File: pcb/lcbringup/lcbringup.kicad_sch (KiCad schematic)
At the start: 4 parts, among them M1 SCREWHOLE, M2 SCREWHOLE, M3 SCREWHOLE, M4 SCREWHOLE

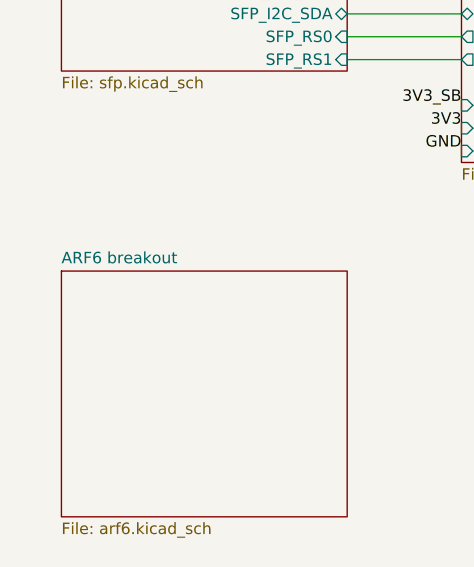
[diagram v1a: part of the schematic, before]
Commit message: Continued lcbringup layout on ARF6 area
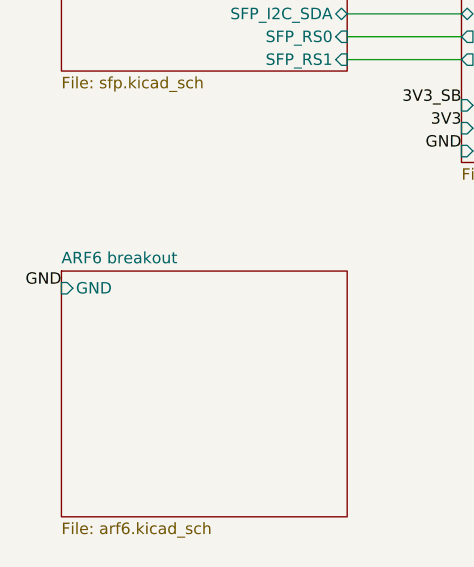
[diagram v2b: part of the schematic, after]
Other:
- sheet ARF6 breakout ports: added GND; removed none
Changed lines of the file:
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@@
 	(title_block
 		(title "Andrew D. Zonenberg")
-		(date "2025-01-14")
+		(date "2025-01-19")
 		(rev "0.1")
 		(company "Antikernel Labs")
@@
 	(label "GND"
 		(at 25.4 111.76 180)
+		(fields_autoplaced yes)
+		(effects
+			(font
+				(size 1.27 1.27)
+			)
+			(justify right bottom)
+		)
+	)
+	(label "GND"
+		(at 25.4 149.86 180)
 		(fields_autoplaced yes)
 		(effects
@@
 			)
 		)
+		(pin "GND" input
+			(at 25.4 149.86 180)
+			(effects
+				(font
+					(size 1.27 1.27)
+				)
+				(justify left)
+			)
+		)

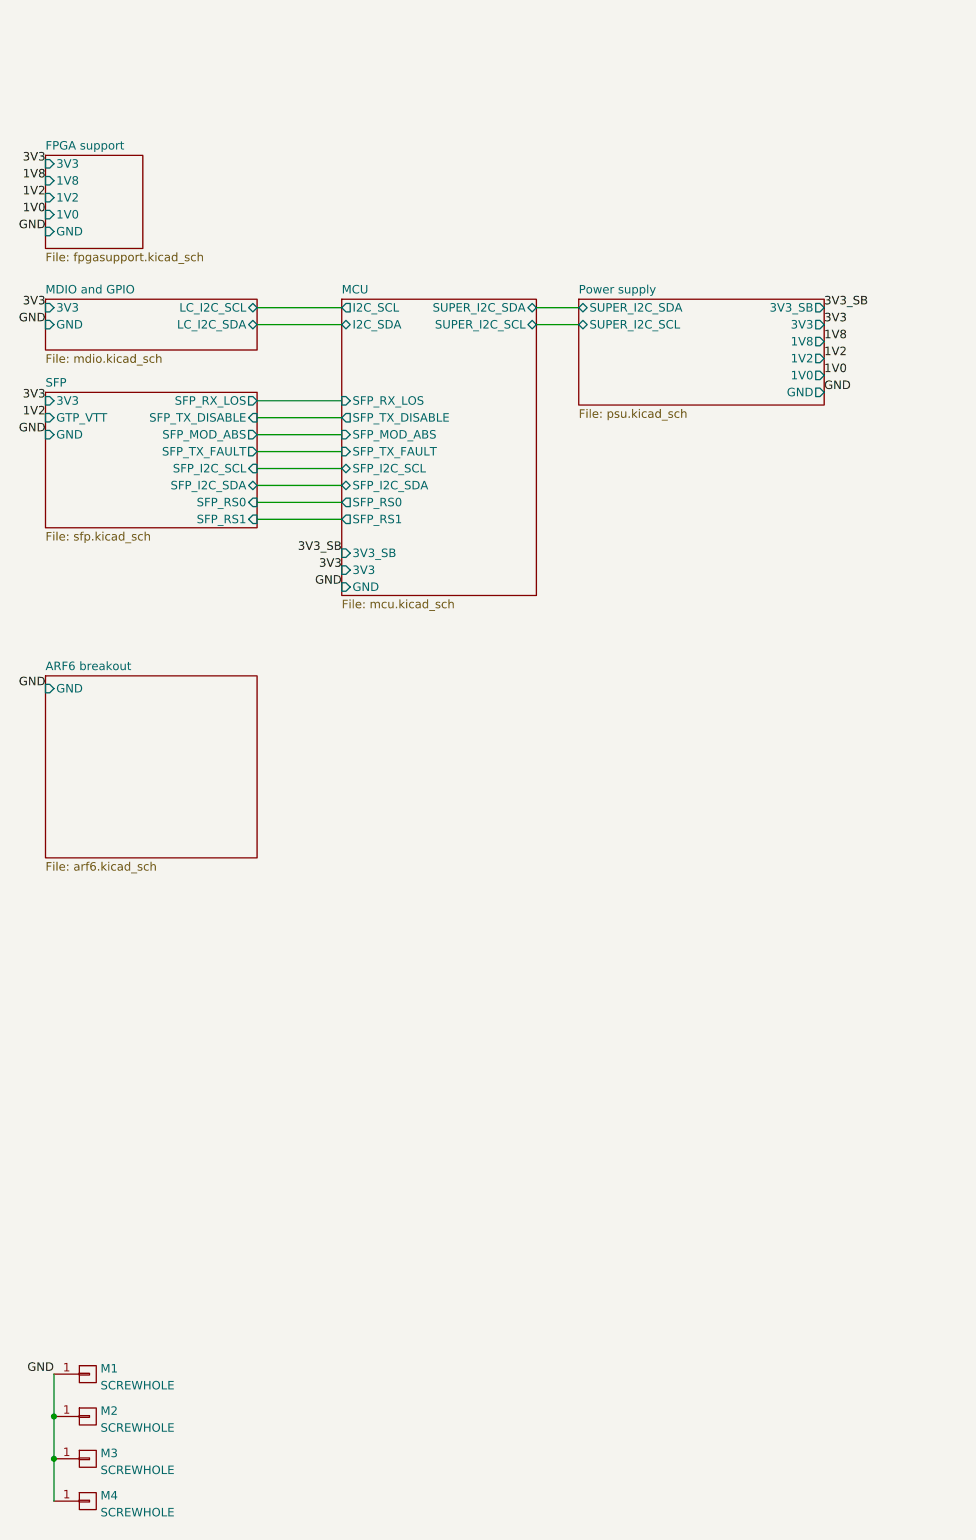
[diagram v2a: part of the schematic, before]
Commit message: Conitnued lcbringup layout, power supply is now floorplanned
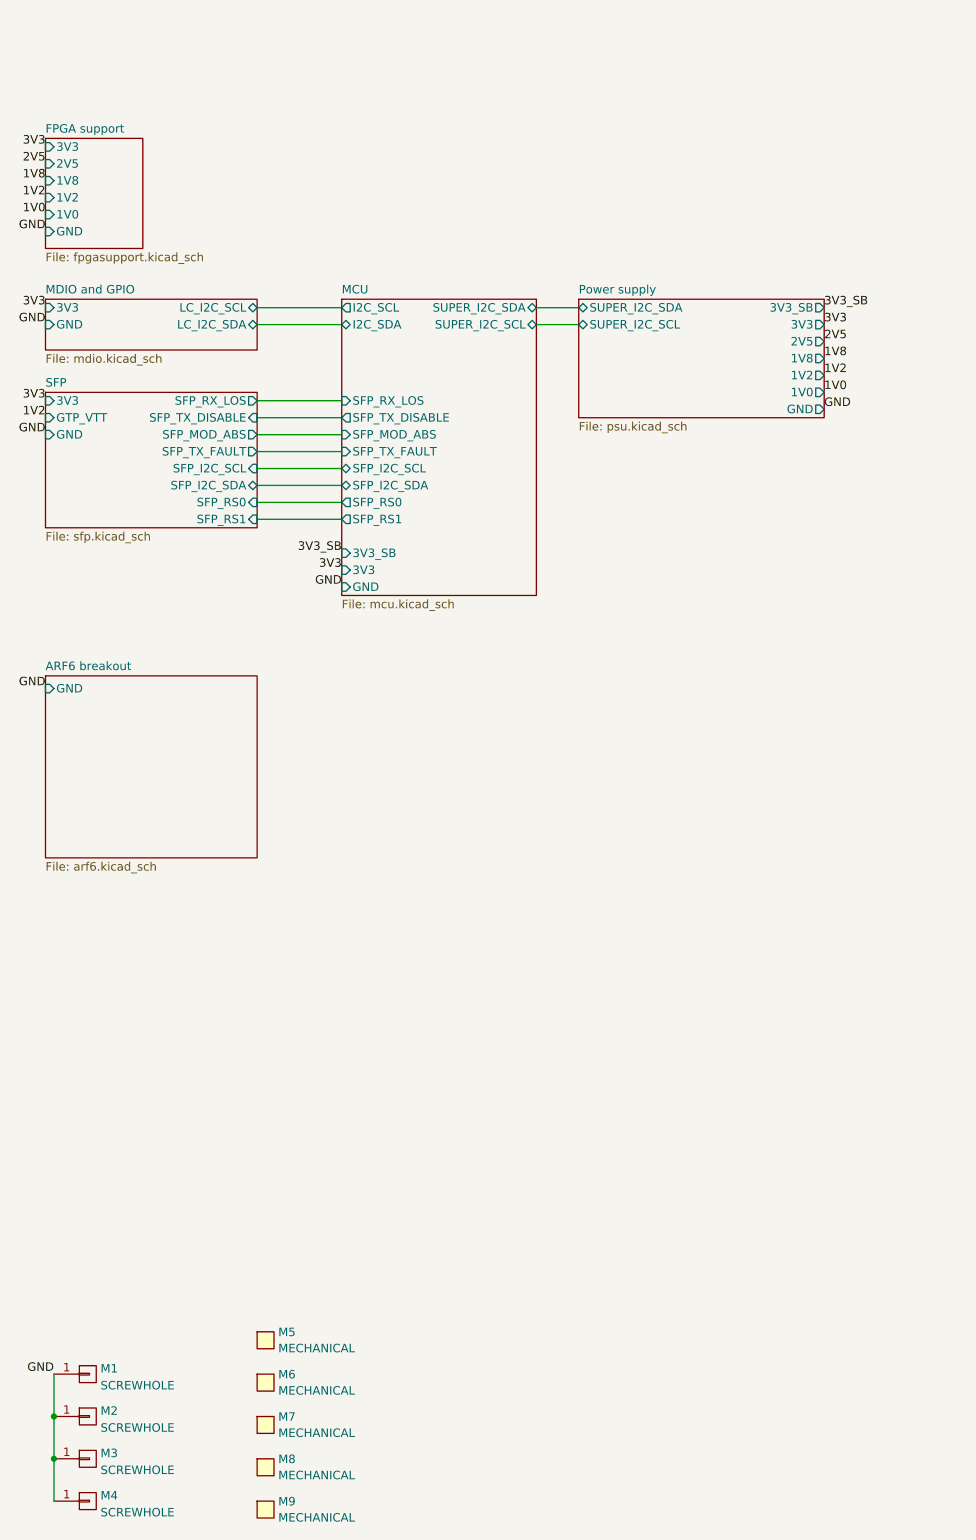
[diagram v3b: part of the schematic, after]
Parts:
- added M5: MECHANICAL, azonenberg_pcb:LONGTHING-1200DPI, symbol special-azonenberg:MECHANICAL
- added M6: MECHANICAL, azonenberg_pcb:LOGO_ESD_SENSITIVE_7MM, symbol special-azonenberg:MECHANICAL
- added M7: MECHANICAL, w_logo:Logo_silk_OSHW_6x6mm, symbol special-azonenberg:MECHANICAL
- added M8: MECHANICAL, w_logo:Logo_silk_ROHS_5x2.8mm, symbol special-azonenberg:MECHANICAL
- added M9: MECHANICAL, w_logo:Logo_silk_WEEE_3.4x5mm, symbol special-azonenberg:MECHANICAL
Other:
- sheet FPGA support ports: added 2V5; removed none
- sheet Power supply ports: added 2V5; removed none

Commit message: Finished lcbringup, ready to order
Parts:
- added TP5: GROUNDCLIP, azonenberg_pcb:TESTPOINT_SMT_KEYSTONE_5016, symbol conn:CONN_01X01
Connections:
- net GND: now also TP5.1 (P1)
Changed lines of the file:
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@@
 	(title_block
 		(title "Andrew D. Zonenberg")
-		(date "2025-01-19")
+		(date "2025-01-20")
 		(rev "0.1")
 		(company "Antikernel Labs")
@@
 	(label "3V3"
 		(at 25.4 106.68 180)
+		(fields_autoplaced yes)
+		(effects
+			(font
+				(size 1.27 1.27)
+			)
+			(justify right bottom)
+		)
+	)
+	(label "GND"
+		(at 26.67 236.22 180)
 		(fields_autoplaced yes)
 		(effects
@@
 					(unit 1)
 				)
+			)
+		)
+	)
+	(symbol
+		(lib_id "conn:CONN_01X01")
+		(at 31.75 236.22 0)
+		(unit 1)
+		(exclude_from_sim no)
+		(in_bom yes)
+		(on_board yes)
+		(dnp no)
+		(fields_autoplaced yes)
+		(property "Reference" "TP5"
+			(at 33.655 235.3853 0)
+			(effects
+				(font
+					(size 1.27 1.27)
+				)
+				(justify left)
+			)
+		)
+		(property "Value" "GROUNDCLIP"
+			(at 33.655 237.9222 0)
+			(effects
+				(font
+					(size 1.27 1.27)
+				)
+				(justify left)
+			)
+		)
+		(property "Footprint" "azonenberg_pcb:TESTPOINT_SMT_KEYSTONE_5016"
+			(at 31.75 236.22 0)
+			(effects
+				(font
+					(size 1.27 1.27)
+				)
+				(hide yes)
+			)
+		)
+		(property "Datasheet" ""
+			(at 31.75 236.22 0)
+			(effects
+				(font
+					(size 1.27 1.27)
+				)
+				(hide yes)
+			)
+		)
+		(property "Description" ""
+			(at 31.75 236.22 0)
+			(effects
+				(font
+					(size 1.27 1.27)
+				)
+				(hide yes)
+			)
+		)
+		(pin "1"
+		)
+		(instances
+			(project "lcbringup"
+				(path "/b833694e-84ba-499b-b91b-2564c6d12291"
+					(reference "TP5")
+					(unit 1)
+				)
